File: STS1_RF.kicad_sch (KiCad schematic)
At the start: 80 parts, among them J1 UHF, Q1 SQ2318, Q3 SQ2318, Q4 SQ2318, U10 TQP3M9036, U11 NL17SV04XV5T2G, U16 F2972, U2 LP2985-1.8, U4 74LVC2G74, U5 TYKTBCSANF-26.000000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

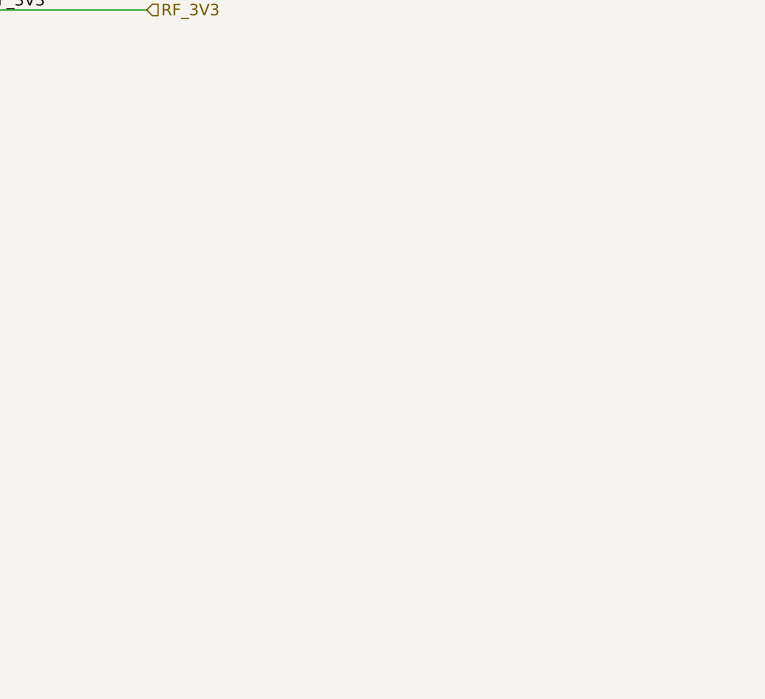
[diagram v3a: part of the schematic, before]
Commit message: Add a temperature sensor near RF amplifier chip
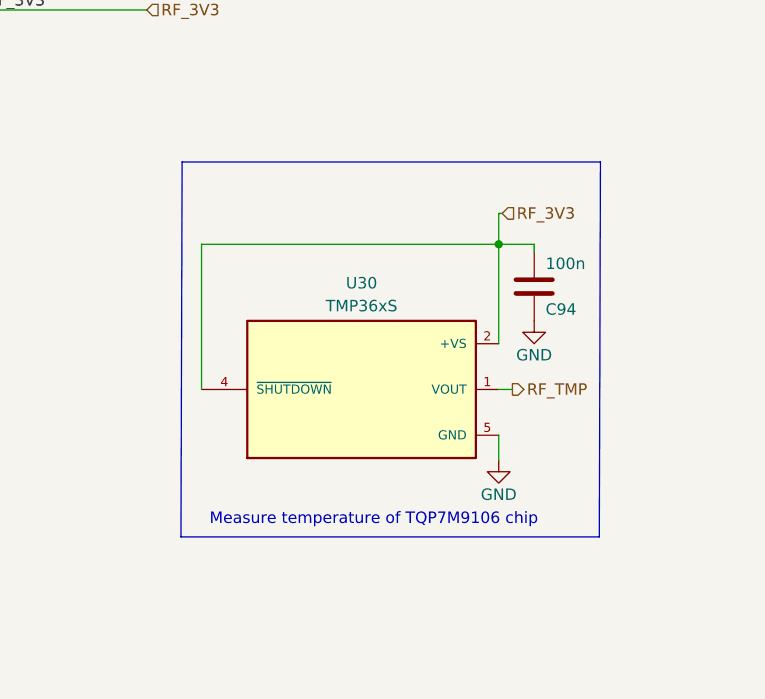
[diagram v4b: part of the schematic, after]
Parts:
- added C94: 100n, Capacitor_SMD:C_0603_1608Metric, symbol Device:C
- added U30: TMP36xS, Package_TO_SOT_SMD:SOT-23-5, symbol STS1_COBC_V2-rescue:TMP36GRTZ-REEL7
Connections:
- net GND: now also C94.1, U30.5 (GND)
- net VCC: now also C94.2, U30.2 (+VS), U30.4 (~{SHUTDOWN})
- new net RF_TMP: U30.1 (VOUT)
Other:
- note added: "Measure temperature of TQP7M9106 chip"
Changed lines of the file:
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@@
   (junction (at 172.72 21.59) (diameter 0) (color 0 0 0 0)
+  )
+  (junction (at 257.556 47.625) (diameter 0) (color 0 0 0 0)
   )
   (junction (at 44.45 125.73) (diameter 0) (color 0 0 0 0)
@@
     (stroke (width 0) (type default) (color 0 0 0 0))
   )
+  (wire (pts (xy 257.556 63.754) (xy 259.08 63.754))
+    (stroke (width 0) (type default) (color 0 0 0 0))
+  )
   (wire (pts (xy 179.07 73.66) (xy 179.07 60.96))
     (stroke (width 0) (type default) (color 0 0 0 0))
@@
     (stroke (width 0) (type default) (color 0 0 0 0))
   )
+  (wire (pts (xy 257.937 44.196) (xy 257.556 44.196))
+    (stroke (width 0) (type default) (color 0 0 0 0))
+  )
   (wire (pts (xy 118.11 68.58) (xy 120.65 68.58))
     (stroke (width 0) (type default) (color 0 0 0 0))
@@
     (stroke (width 0) (type default) (color 0 0 0 0))
   )
+  (wire (pts (xy 224.536 47.625) (xy 257.556 47.625))
+    (stroke (width 0) (type default) (color 0 0 0 0))
+  )
   (wire (pts (xy 46.99 99.06) (xy 49.53 99.06))
     (stroke (width 0) (type default) (color 0 0 0 0))
@@
     (stroke (width 0) (type default) (color 0 0 0 0))
   )
+  (wire (pts (xy 261.493 47.625) (xy 257.556 47.625))
+    (stroke (width 0) (type default) (color 0 0 0 0))
+  )
+  (polyline (pts (xy 222.377 38.481) (xy 222.25 80.137))
+    (stroke (width 0) (type default) (color 0 0 0 0))
+  )
   (wire (pts (xy 264.16 101.6) (xy 264.16 104.14))
     (stroke (width 0) (type default) (color 0 0 0 0))
@@
     (stroke (width 0) (type default) (color 0 0 0 0))
   )
+  (polyline (pts (xy 222.25 80.137) (xy 268.732 80.137))
+    (stroke (width 0) (type default) (color 0 0 0 0))
+  )
   (wire (pts (xy 118.11 76.2) (xy 120.65 76.2))
     (stroke (width 0) (type default) (color 0 0 0 0))
@@
     (stroke (width 0) (type default) (color 0 0 0 0))
   )
+  (wire (pts (xy 257.556 47.625) (xy 257.556 58.674))
+    (stroke (width 0) (type default) (color 0 0 0 0))
+  )
   (wire (pts (xy 158.75 60.96) (xy 166.37 60.96))
     (stroke (width 0) (type default) (color 0 0 0 0))
@@
     (stroke (width 0) (type default) (color 0 0 0 0))
   )
+  (polyline (pts (xy 268.732 80.137) (xy 268.859 38.481))
+    (stroke (width 0) (type default) (color 0 0 0 0))
+  )
   (wire (pts (xy 66.04 43.18) (xy 82.55 43.18))
     (stroke (width 0) (type default) (color 0 0 0 0))
@@
     (stroke (width 0) (type default) (color 0 0 0 0))
   )
+  (wire (pts (xy 224.536 63.754) (xy 224.536 47.625))
+    (stroke (width 0) (type default) (color 0 0 0 0))
+  )
   (wire (pts (xy 39.37 146.05) (xy 39.37 137.16))
     (stroke (width 0) (type default) (color 0 0 0 0))
   )
+  (wire (pts (xy 257.556 68.834) (xy 257.556 71.628))
+    (stroke (width 0) (type default) (color 0 0 0 0))
+  )
   (wire (pts (xy 165.1 50.8) (xy 172.72 50.8))
     (stroke (width 0) (type default) (color 0 0 0 0))
@@
     (stroke (width 0) (type default) (color 0 0 0 0))
   )
+  (wire (pts (xy 261.493 48.514) (xy 261.493 47.625))
+    (stroke (width 0) (type default) (color 0 0 0 0))
+  )
   (wire (pts (xy 130.81 21.59) (xy 130.81 45.72))
     (stroke (width 0) (type default) (color 0 0 0 0))
@@
     (stroke (width 0) (type default) (color 0 0 0 0))
   )
+  (polyline (pts (xy 222.377 38.481) (xy 268.859 38.481))
+    (stroke (width 0) (type default) (color 0 0 0 0))
+  )
   (wire (pts (xy 58.42 116.84) (xy 60.96 116.84))
     (stroke (width 0) (type default) (color 0 0 0 0))
@@
   )
   (wire (pts (xy 240.03 140.97) (xy 245.11 140.97))
+    (stroke (width 0) (type default) (color 0 0 0 0))
+  )
+  (wire (pts (xy 257.556 44.196) (xy 257.556 47.625))
     (stroke (width 0) (type default) (color 0 0 0 0))
   )
@@
     (effects (font (size 1.27 1.27)) (justify left bottom))
   )
+  (text "Measure temperature of TQP7M9106 chip" (at 225.425 78.994 0)
+    (effects (font (size 1.27 1.27)) (justify left bottom))
+  )
   (label "RF_3V3" (at 200.66 21.59 0)
     (effects (font (size 1.27 1.27)) (justify left bottom))
@@
     (effects (font (size 1.27 1.27)) (justify right bottom))
   )
+  (hierarchical_label "RF_3V3" (shape input) (at 257.937 44.196 0)
+    (effects (font (size 1.27 1.27)) (justify left))
+  )
   (hierarchical_label "GPIO0" (shape bidirectional) (at 143.51 68.58 0)
+    (effects (font (size 1.27 1.27)) (justify left))
+  )
+  (hierarchical_label "RF_TMP" (shape output) (at 259.08 63.754 0)
     (effects (font (size 1.27 1.27)) (justify left))
   )
@@
     )
     (property "Datasheet" "" (id 3) (at 34.29 109.22 0)
+      (effects (font (size 1.27 1.27)) hide)
+    )
+    (pin "1")
+  )
+  (symbol (lib_id "power:GND") (at 257.556 71.628 0) (unit 1)
+    (in_bom yes) (on_board yes)
+    (property "Reference" "#PWR062" (id 0) (at 257.556 77.978 0)
+      (effects (font (size 1.27 1.27)) hide)
+    )
+    (property "Value" "GND" (id 1) (at 257.556 75.438 0))
+    (property "Footprint" "" (id 2) (at 257.556 71.628 0)
+      (effects (font (size 1.27 1.27)) hide)
+    )
+    (property "Datasheet" "" (id 3) (at 257.556 71.628 0)
       (effects (font (size 1.27 1.27)) hide)
     )
@@
     (pin "2")
   )
+  (symbol (lib_id "STS1_COBC_V2-rescue:TMP36GRTZ-REEL7") (at 242.316 63.754 0) (unit 1)
+    (in_bom yes) (on_board yes)
+    (property "Reference" "U30" (id 0) (at 242.316 51.943 0))
+    (property "Value" "TMP36xS" (id 1) (at 242.316 54.483 0))
+    (property "Footprint" "Package_TO_SOT_SMD:SOT-23-5" (id 2) (at 243.586 95.504 0)
+      (effects (font (size 1.27 1.27)) (justify bottom) hide)
+    )
+    (property "Datasheet" "https://www.analog.com/media/en/technical-documentation/data-sheets/TMP35_36_37.pdf" (id 3) (at 242.316 63.754 0)
+      (effects (font (size 1.27 1.27)) hide)
+    )
+    (property "MF" "Analog Devices" (id 4) (at 242.316 87.884 0)
+      (effects (font (size 1.27 1.27)) (justify bottom) hide)
+    )
+    (property "Description" "\nVoltage Output Temperature Sensors\n" (id 5) (at 242.316 63.754 0)
+      (effects (font (size 1.27 1.27)) (justify bottom) hide)
+    )
+    (property "Package" "SOT-5 Analog Devices" (id 6) (at 243.586 92.964 0)
+      (effects (font (size 1.27 1.27)) (justify bottom) hide)
+    )
+    (property "Price" "None" (id 7) (at 242.316 90.424 0)
+      (effects (font (size 1.27 1.27)) (justify bottom) hide)
+    )
+    (property "STANDARD" "IPC-7351B" (id 8) (at 242.316 63.754 0)
+      (effects (font (size 1.27 1.27)) (justify bottom) hide)
+    )
+    (property "PARTREV" "H" (id 9) (at 243.586 98.044 0)
+      (effects (font (size 1.27 1.27)) (justify bottom) hide)
+    )
+    (property "SnapEDA_Link" "https://www.snapeda.com/parts/TMP36GRTZ-REEL7/Analog+Devices/view-part/?ref=snap" (id 10) (at 244.856 82.804 0)
+      (effects (font (size 1.27 1.27)) (justify bottom) hide)
+    )
+    (property "MP" "TMP36GRTZ-REEL7" (id 11) (at 242.316 54.864 0)
+      (effects (font (size 1.27 1.27)) (justify bottom) hide)
+    )
+    (property "Purchase-URL" "https://www.snapeda.com/api/url_track_click_mouser/?unipart_id=46170&manufacturer=Analog Devices&part_name=TMP36GRTZ-REEL7&search_term=tmp36grtz" (id 12) (at 243.586 101.854 0)
+      (effects (font (size 1.27 1.27)) (justify bottom) hide)
+    )
+    (property "Availability" "In Stock" (id 13) (at 242.316 99.314 0)
+      (effects (font (size 1.27 1.27)) (justify bottom) hide)
+    )
+    (property "Check_prices" "https://www.snapeda.com/parts/TMP36GRTZ-REEL7/Analog+Devices/view-part/?ref=eda" (id 14) (at 244.856 85.344 0)
+      (effects (font (size 1.27 1.27)) (justify bottom) hide)
+    )
+    (pin "1")
+    (pin "2")
+    (pin "4")
+    (pin "5")
+  )
   (symbol (lib_id "Device:C") (at 161.29 50.8 90) (unit 1)
     (in_bom yes) (on_board yes)
@@
     (pin "4")
     (pin "5")
+  )
+  (symbol (lib_id "Device:C") (at 261.493 52.324 180) (unit 1)
+    (in_bom yes) (on_board yes)
+    (property "Reference" "C94" (id 0) (at 262.763 54.864 0)
+      (effects (font (size 1.27 1.27)) (justify right))
+    )
+    (property "Value" "100n" (id 1) (at 262.763 49.784 0)
+      (effects (font (size 1.27 1.27)) (justify right))
+    )
+    (property "Footprint" "Capacitor_SMD:C_0603_1608Metric" (id 2) (at 260.5278 48.514 0)
+      (effects (font (size 1.27 1.27)) hide)
+    )
+    (property "Datasheet" "~" (id 3) (at 261.493 52.324 0)
+      (effects (font (size 1.27 1.27)) hide)
+    )
+    (pin "1")
+    (pin "2")
   )
   (symbol (lib_id "power:GND") (at 166.37 76.2 0) (unit 1)
@@
     (pin "9")
   )
+  (symbol (lib_id "power:GND") (at 261.493 56.134 0) (unit 1)
+    (in_bom yes) (on_board yes)
+    (property "Reference" "#PWR061" (id 0) (at 261.493 62.484 0)
+      (effects (font (size 1.27 1.27)) hide)
+    )
+    (property "Value" "GND" (id 1) (at 261.493 59.944 0))
+    (property "Footprint" "" (id 2) (at 261.493 56.134 0)
+      (effects (font (size 1.27 1.27)) hide)
+    )
+    (property "Datasheet" "" (id 3) (at 261.493 56.134 0)
+      (effects (font (size 1.27 1.27)) hide)
+    )
+    (pin "1")
+  )
   (symbol (lib_id "power:GND") (at 149.86 156.21 0) (unit 1)

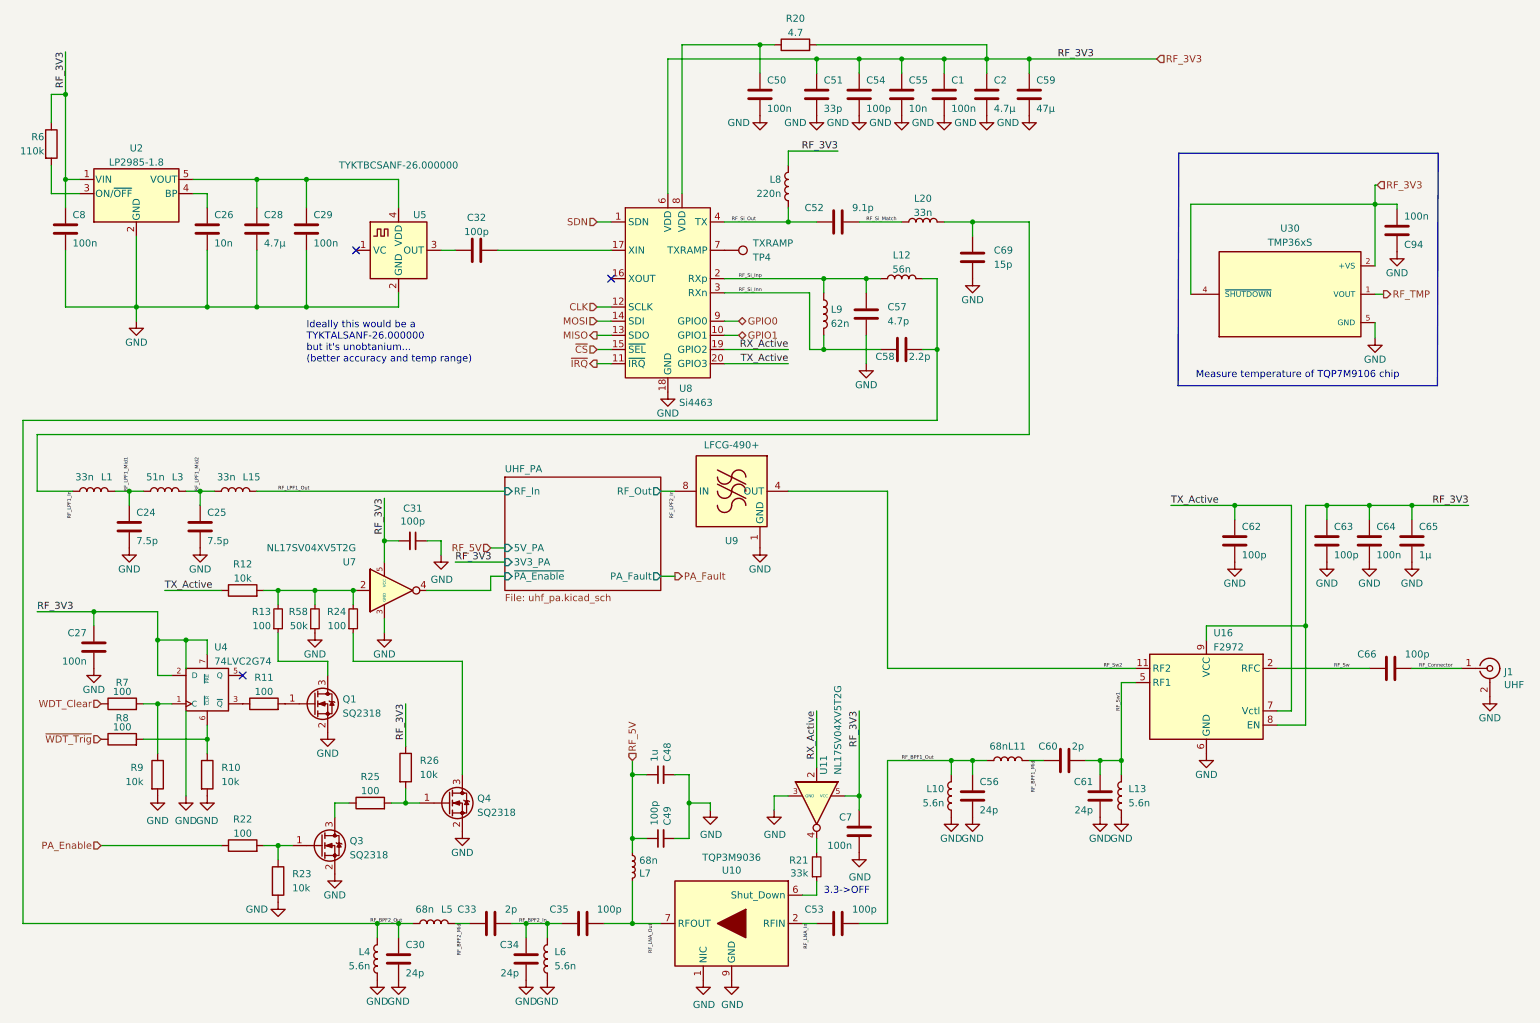
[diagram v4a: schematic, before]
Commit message: Add manufacture number and JLCPCB part number to components
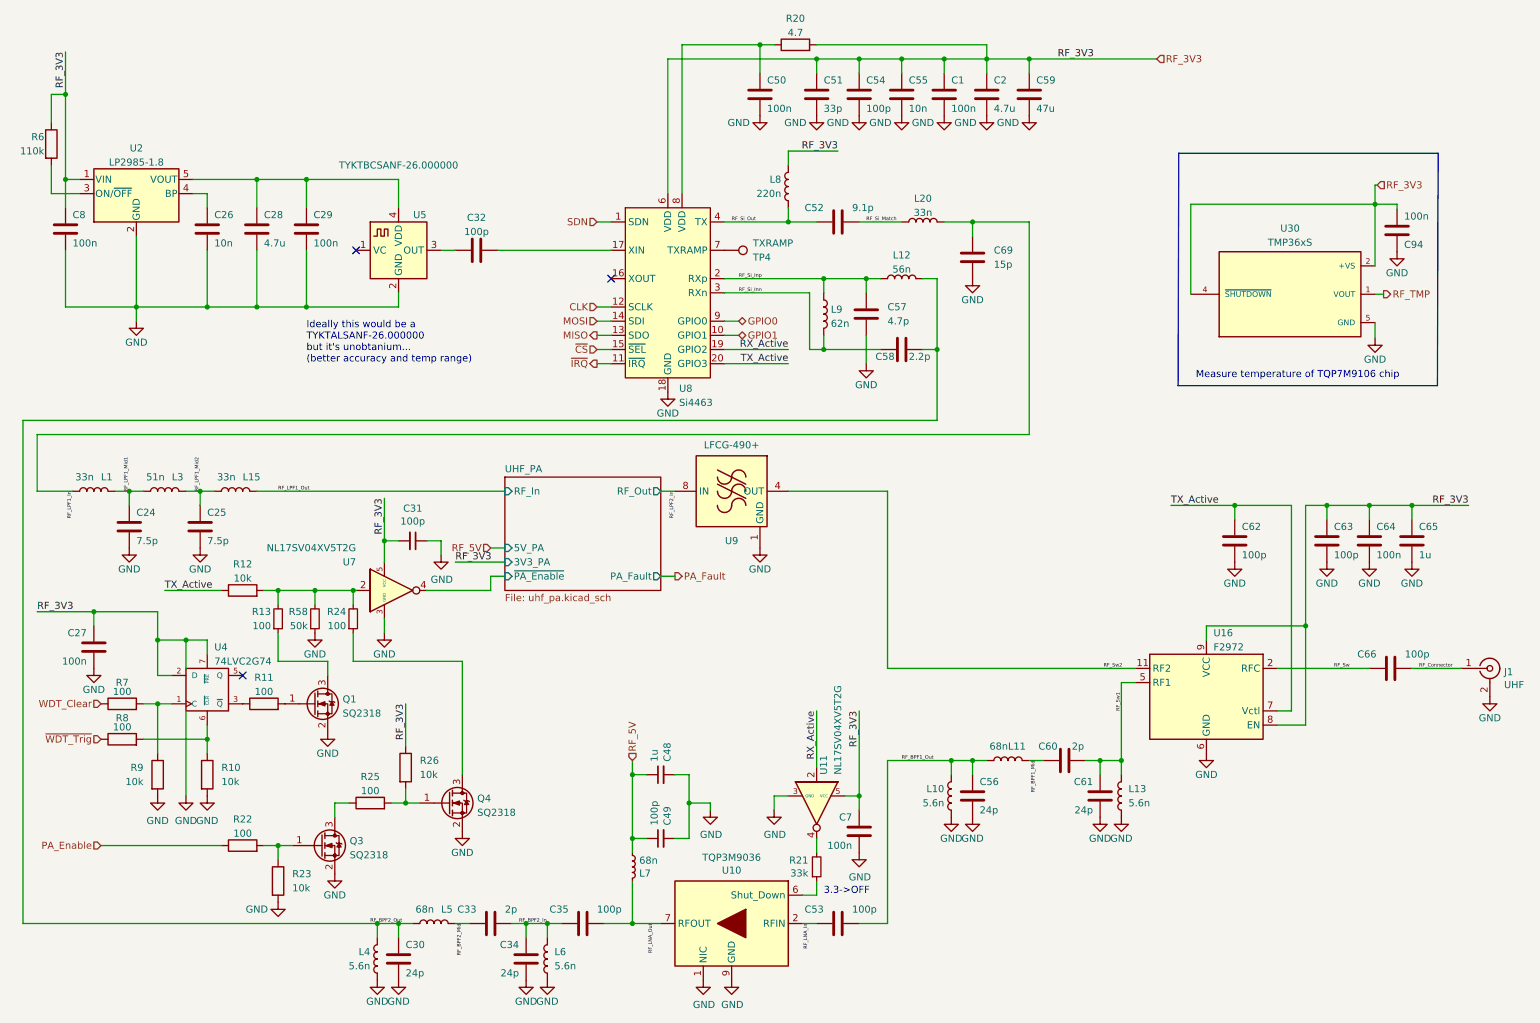
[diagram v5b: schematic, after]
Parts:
- C1, C27, C29, C50, C64, C7, C8: JLCPCB Part # (none) -> C1711; Manufacturer_Part_Number (none) -> CL21B104KBCNNNC
- C2, C28: value 4.7µ -> 4.7u; JLCPCB Part # (none) -> C722528; Manufacturer_Part_Number (none) -> CL21A475KAQNNNG
- C24, C25: JLCPCB Part # (none) -> C3864905; Manufacturer_Part_Number (none) -> VJ0402D7R5CXAAJHT
- C26, C55: JLCPCB Part # (none) -> C7224472; Manufacturer_Part_Number (none) -> C0805C103K8RACAUTO
- C30, C34, C56, C61: JLCPCB Part # (none) -> C3833393; Manufacturer_Part_Number (none) -> UMK105CG240JV-F
- C31, C32, C35, C49, C53, C54, C62, C63, C66: JLCPCB Part # (none) -> C386123; Manufacturer_Part_Number (none) -> UMK105CG101JV-F
- C33, C60: JLCPCB Part # (none) -> C76962; Manufacturer_Part_Number (none) -> GRM1555C1H2R0CA01D
- C48: Manufacturer_Part_Number (none) -> C0402C105K8PAC7411
- C51: JLCPCB Part # (none) -> C70465; Manufacturer_Part_Number (none) -> CL05C330JB5NNNC
- C52: JLCPCB Part # (none) -> C3908063; Manufacturer_Part_Number (none) -> RF15N9R1B500CT
- C57: JLCPCB Part # (none) -> C5534411; Manufacturer_Part_Number (none) -> 885392005012
- C58: JLCPCB Part # (none) -> C172819; Manufacturer_Part_Number (none) -> RF15N2R2B500CT
- C59: value 47µ -> 47u; Manufacturer_Part_Number (none) -> CL21A476MQYNNWE
- C65: value 1µ -> 1u; Manufacturer_Part_Number (none) -> C0402C105K8PAC7411
- C69: Manufacturer_Part_Number (none) -> 500R07S150KV4T
- C94: JLCPCB Part # (none) -> C1591; Manufacturer_Part_Number (none) -> CL10B104KB8NNNC
- J1: JLCPCB Part # (none) -> C6095037; Manufacturer_Part_Number (none) -> 61612002121503
- L1, L15, L20: JLCPCB Part # (none) -> C2043918; Manufacturer_Part_Number (none) -> LQW15AN33NJ8ZD
- L10, L13, L4, L6: Manufacturer_Part_Number (none) -> LQW15AN5N6C1ZD
- L11, L5, L7: JLCPCB Part # (none) -> C2049784; Manufacturer_Part_Number (none) -> LQW15AN68NJ0ZD
- L12: Manufacturer_Part_Number (none) -> LQW15AN56NH0ZD
- L3: Manufacturer_Part_Number (none) -> LQW15AN51NG80D
- L8: JLCPCB Part # (none) -> C341690; Manufacturer_Part_Number (none) -> LQW15CNR22J10D
- L9: Manufacturer_Part_Number (none) -> LQW15AN62NJ0ZD
- Q1, Q3, Q4: JLCPCB Part # (none) -> C3280170; Manufacturer_Part_Number (none) -> SQ2318AES-T1_BE3
- R10, R12, R23, R26, R9: JLCPCB Part # (none) -> C4297913; Manufacturer_Part_Number (none) -> ERJ-H3EF1002V
- R11, R13, R22, R24, R25, R7, R8: JLCPCB Part # (none) -> C2074896; Manufacturer_Part_Number (none) -> CRS0603AFX-1000ELF
- R20: Manufacturer_Part_Number (none) -> CHP0603QFW-4R70ELF
- R21: JLCPCB Part # (none) -> C4220470; Manufacturer_Part_Number (none) -> ERJ-H3EF3302V
- R6: JLCPCB Part # (none) -> C4176290; Manufacturer_Part_Number (none) -> ERJ-H3EF1103V
- U10: JLCPCB Part # (none) -> C920261; Manufacturer_Part_Number (none) -> TQP3M9036
- U11, U7: JLCPCB Part # (none) -> C185507; Manufacturer_Part_Number (none) -> NL17SV04XV5T2G
- U16: JLCPCB Part # (none) -> C1558621; Manufacturer_Part_Number (none) -> F2972NEGK
- U2: JLCPCB Part # (none) -> C3752498; Manufacturer_Part_Number (none) -> LP2985-18DBVRE4
- U30: JLCPCB Part # (none) -> C129489; Manufacturer_Part_Number (none) -> TMP36GRTZ-REEL7
- U4: JLCPCB Part # (none) -> C3826121; Manufacturer_Part_Number (none) -> SN74LVC2G74DCUTE4
- U5: JLCPCB Part # (none) -> C6304737; Manufacturer_Part_Number (none) -> TYKTBCSANF-26.000000
- U8: JLCPCB Part # (none) -> C476202; Manufacturer_Part_Number (none) -> SI4463-C2A-GM
- U9: JLCPCB Part # (none) -> C3034233; Manufacturer_Part_Number (none) -> LFCG-490+
